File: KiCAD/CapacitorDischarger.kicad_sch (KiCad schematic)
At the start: 44 parts, among them J1 SLB4-G-21, J2 SLB4-G-22, J3 MKDS5/2-9.5, J4 MKDS5/2-9.5, J5 DVM_Connector, Q1 MPSA42, Q2 STP10NK80Z 800V 9A

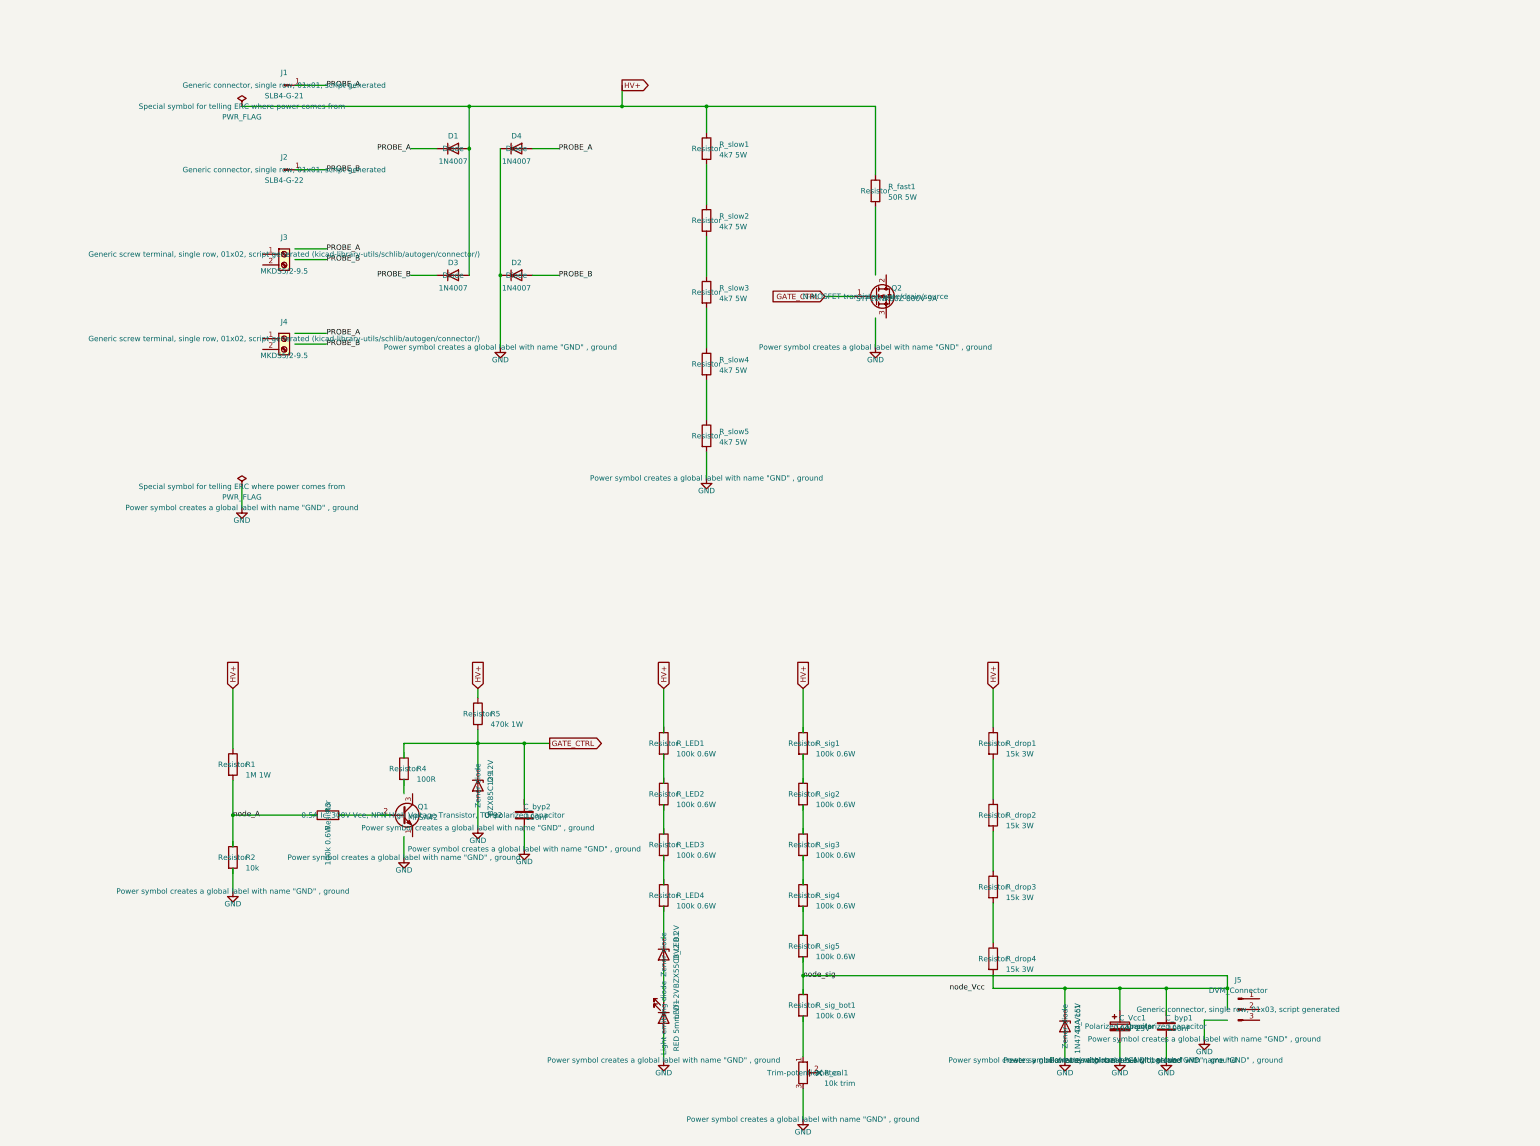
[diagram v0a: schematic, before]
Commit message: Design review fixes: fuse F1, battery-powered DVM, R3=10k, KiCad polarity fixes
Review of the full design (schematic, BOM, simulations) surfaced and fixed:

- Add F1 protection fuse (2A/600V KLKD002.T + Keystone 3517 clips) in
  series after the bridge — opens on single-fault Q2-stuck-on (~12A).
- Reduce R3 100k -> 10k: Q1 threshold now hFE-independent, 63V nominal /
  68V at the BF=40 corner (was 76V / 154V, peak I_fast ~3A over the 2A
  PCB limit).
- Replace the DVM Vcc parasitic dropper (4x15k + 1N4744A) with a 9V
  battery (BT1, holder w/ switch) via new polarized JST XH input J6:
  the sourced DVM module measures 12-15mA, beyond the dropper's 9.75mA.
- Fix gate-drive drawing in the generated schematic: D9 is a shunt clamp
  at GATE_CTRL, not in series (SVG previously showed a broken topology).
- KiCad root schematic: bridge D1-D4 and LED1 were mounted reversed —
  rotated 180 (netlist-verified); F1 and J6 added, dropper removed,
  VCC_DVM rail unshorted from node_sig, C_byp1 pins actually connected;
  value fields R3/R5/R_fast corrected; section drafts updated to match.
- Simulations: bridge D1-D4 now modeled (residual ~1V verified), MOSFET
  model renamed to STP10NK80Z, low-hFE threshold corner scenario G2
  added, Vcc branch removed with the dropper; suite passes 8/8.
- BOM/README: regenerate stale bom.md (Q1=MPSA42, 4x R_LED, 10k R_cal),
  correct stress-math notes, document residual voltage, threshold range,
  discharge time 45.5s @ 600V/1mF, and high-efficiency LED requirement.

Co-Authored-By: Claude Fable 5 <noreply@anthropic.com>
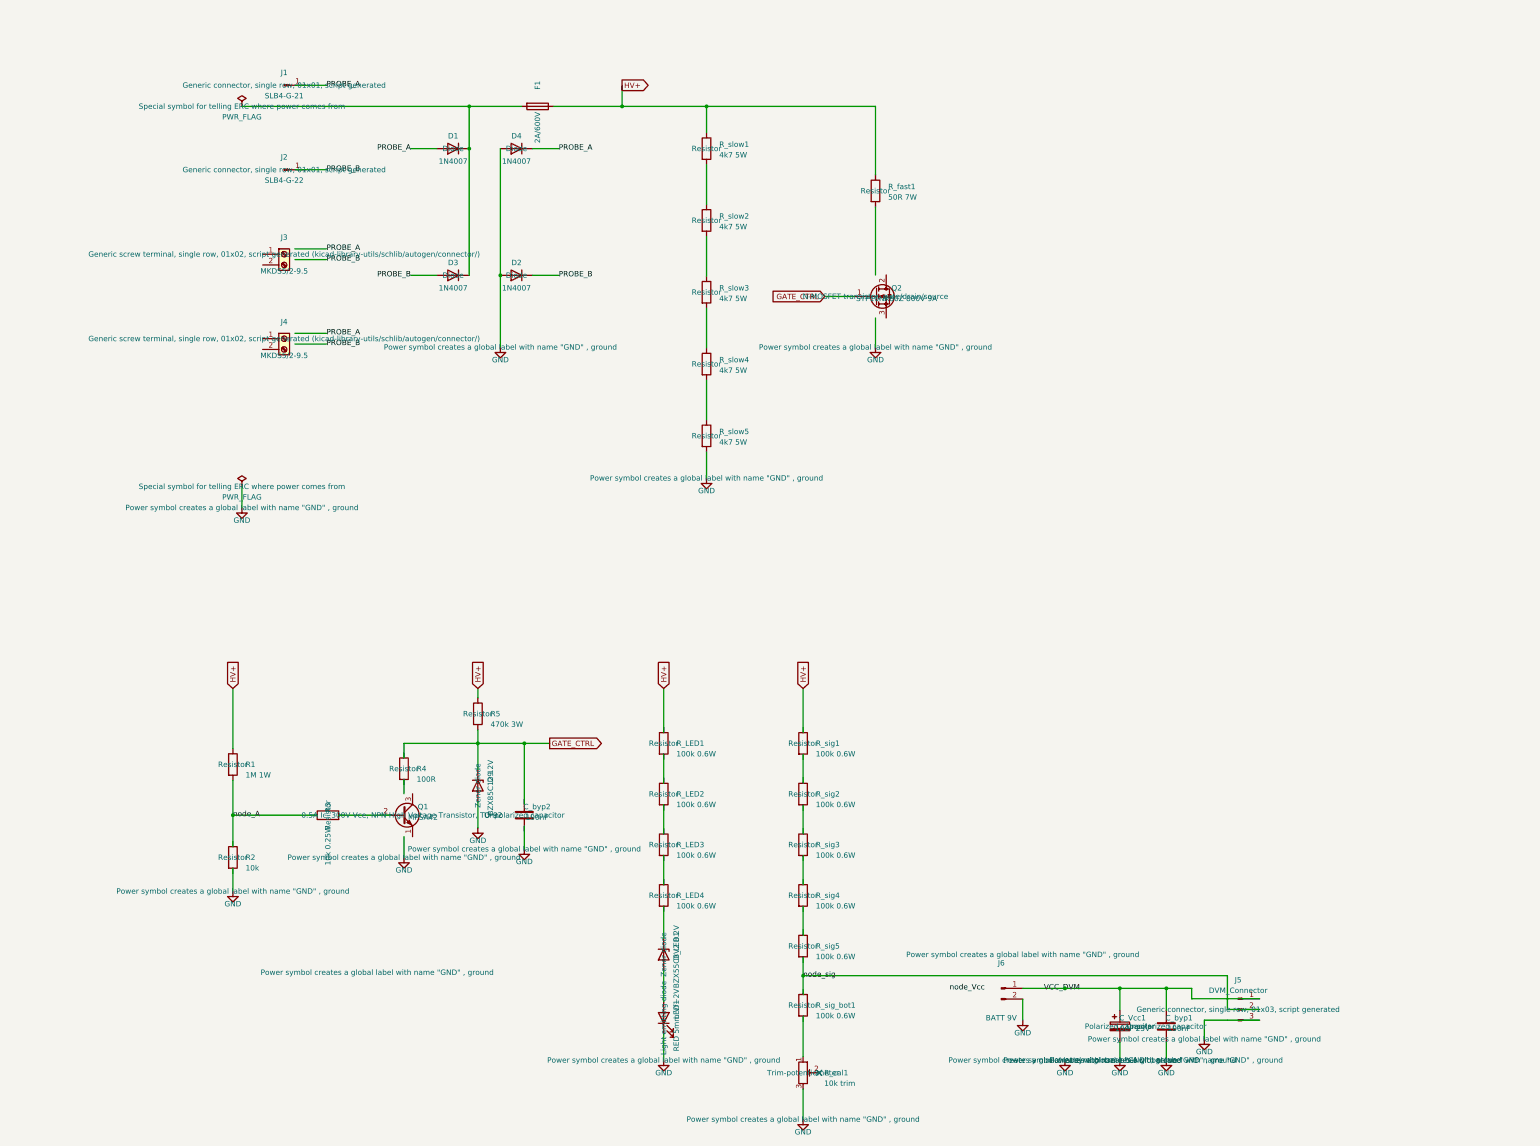
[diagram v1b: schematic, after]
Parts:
- removed D_Vcc1: 1N4744A 15V, Diode_THT:D_DO-41_SOD81_P10.16mm_Horizontal, symbol Device:D_Zener
- removed R_drop1, R_drop2, R_drop3, R_drop4: 15k 3W, Resistor_THT:R_Axial_DIN0516_L15.5mm_D5.0mm_P20.32mm_Horizontal, symbol Device:R
- added F1: 2A/600V, Fuse:Fuseholder_Clip-6.3x32mm_Littelfuse_102_Inline_P34.21x7.62mm_D2.54mm_Horizontal, symbol Device:Fuse
- added J6: BATT 9V, Connector_JST:JST_XH_B2B-XH-A_1x02_P2.50mm_Vertical, symbol Connector:Conn_01x02_Pin
- R3: value 100k 0.6W -> 10k 0.25W
- R5: value 470k 1W -> 470k 3W
- R_fast1: value 50R 5W -> 50R 7W
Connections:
- net GND: now also C_byp1.2, D2.2 (A), D4.2 (A), J5.3 (Pin_3), LED1.1 (K), J6.2 (Pin_2); no longer D2.1 (K), D4.1 (K), LED1.2 (A)
- net HV+: now also F1.2; no longer D1.2 (A), D3.2 (A)
- net PROBE_A: now also D1.2 (A), D4.1 (K); no longer D1.1 (K), D4.2 (A)
- net PROBE_B: now also D2.1 (K), D3.2 (A); no longer D2.2 (A), D3.1 (K)
- net node_sig: now also J5.2 (Pin_2); no longer C_Vcc1.1
- net at D_LED1.2 (A): now also LED1.2 (A); no longer LED1.1 (K)
- net VCC_DVM: now reaches C_byp1.1
- net VCC_DVM: now also C_Vcc1.1, J5.1 (Pin_1), J6.1 (Pin_1)
- new net: D1.1 (K), D3.1 (K), F1.1
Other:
- moved on the sheet: D1, D2, D3, D4, LED1

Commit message: Design review fixes, PM-128 voltmeter, TF1 cutoff, regenerated KiCad project
Circuit / simulation
- Add TF1 thermal cutoff (SEFUSE SF129R0, 133 °C) between R_fast and Q2;
  behavioural thermal model in the sim, live-supply scenario L
- Replace the 0-100 V DVM module with an Axiomet PM-128 (200 mV FS) on a
  10 000:1 divider (5 x 100k over 2 x 100R), D_clamp input protection,
  floating 9 V battery
- New scenarios: hFE/temperature corners (G3/G4), PM-128 divider (H),
  reverse polarity (I), hot-plug (J), 47 mF dump (K), live supply (L);
  run_sim fails on any ngspice error; 15/15 PASS

BOM
- F1 = ESKA 1038820 + Schurter CSO clips, R_sig_bot = 2 x 100R, HLMP-4700,
  HS-S01 heatsink, MST 220 insulator, wire, enclosure; TO_BUY_list.csv

KiCad (all generated by scripts in KiCAD/)
- gen_kicad_sch.py: flat schematic, netlist checked against the SPICE
  circuit by check_kicad.py (ERC clean)
- hv_rules.py: clearance = 1 mm per 100 V of worst-case voltage difference
  (6 mm HV to GND/LV)
- gen_pcb.py: 2-layer board 120 x 90 mm, Freerouting with per-net classes
- board_1s.py: single-sided 100 x 75 mm board for Bungard FEPCU-075,
  hand-routed, GND ring, no jumpers; fab_1s/ exposure PDF, drill, STEP
- gen_footprints.py / gen_3d.py: custom footprints and STEP bodies
- Remove the old hv_section / lv_section drafts

Co-Authored-By: Claude Opus 5.5 (1M context) <noreply@anthropic.com>
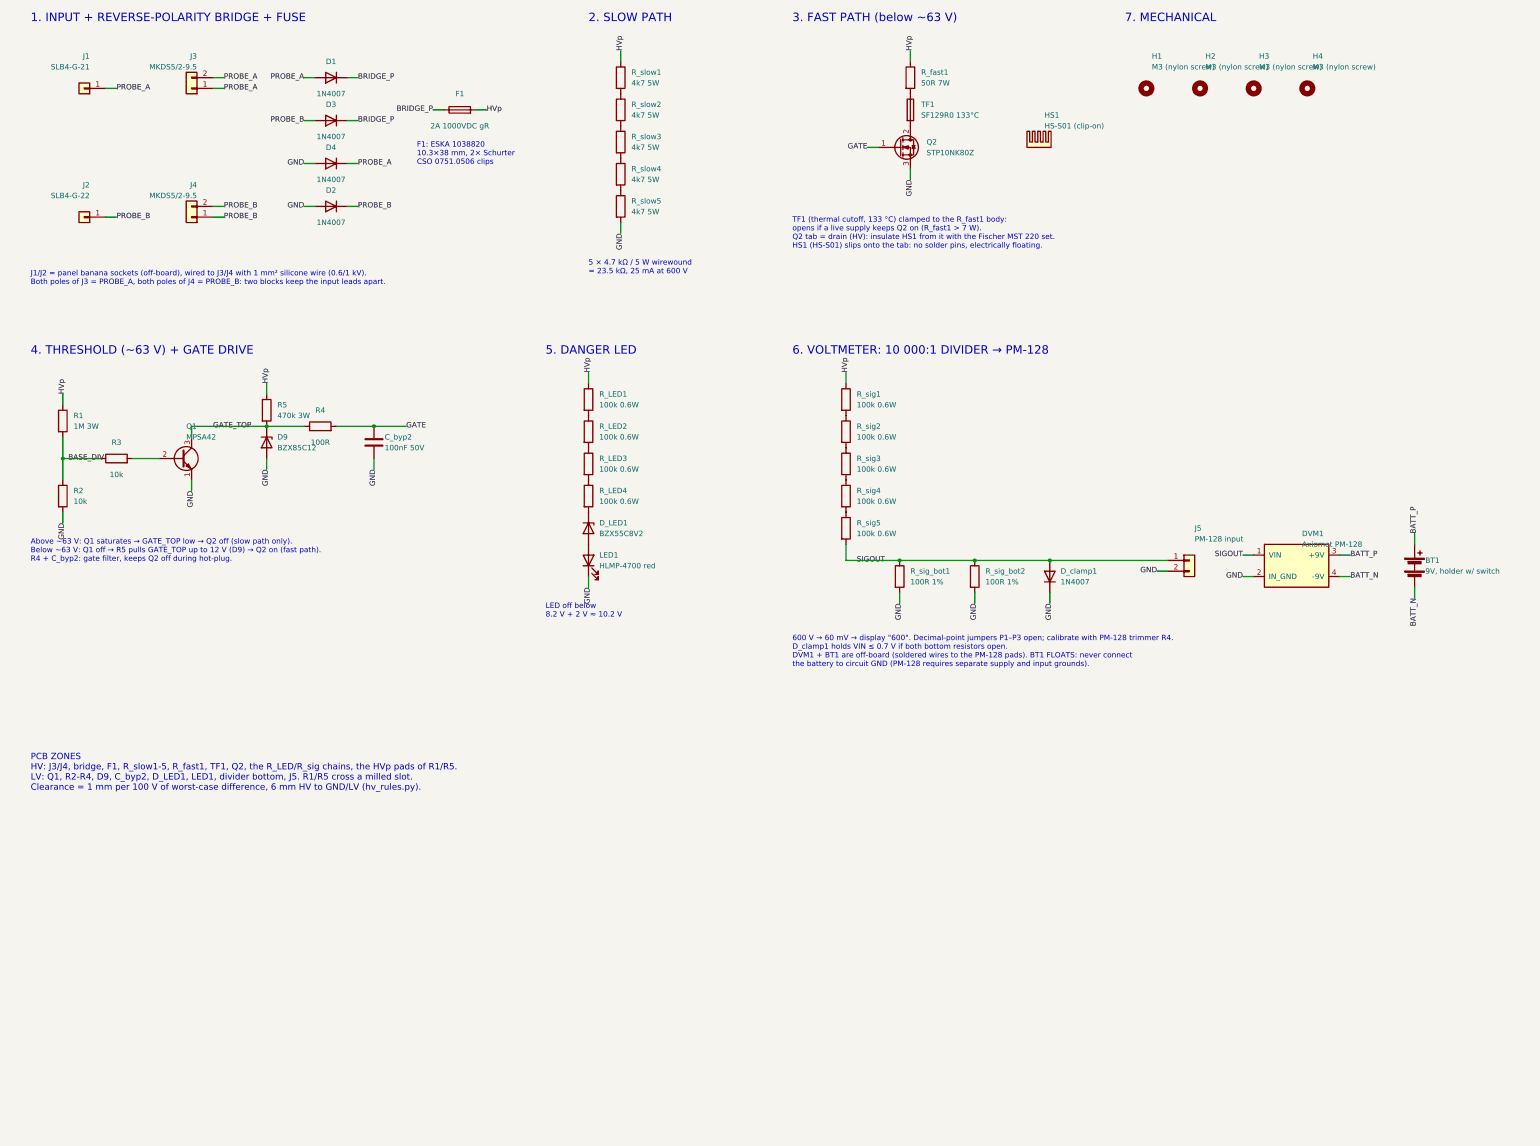
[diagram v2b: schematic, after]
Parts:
- removed C_Vcc1: 10uF 25V, Capacitor_THT:CP_Radial_D4.0mm_P2.00mm, symbol Device:C_Polarized
- removed C_byp1: 100nF, Capacitor_THT:C_Disc_D3.8mm_W2.6mm_P2.50mm, symbol Device:C
- removed J1: SLB4-G-21, Connector_PinHeader_2.54mm:PinHeader_1x01_P2.54mm_Vertical, symbol Connector:Conn_01x01_Pin
- removed J2: SLB4-G-22, Connector_PinHeader_2.54mm:PinHeader_1x01_P2.54mm_Vertical, symbol Connector:Conn_01x01_Pin
- removed J3, J4: MKDS5/2-9.5, TerminalBlock_Phoenix:TerminalBlock_Phoenix_MKDS-1,5-2_1x02_P5.00mm_Horizontal, symbol Connector:Screw_Terminal_01x02
- removed J5: DVM_Connector, Connector_PinHeader_2.54mm:PinHeader_1x03_P2.54mm_Vertical, symbol Connector:Conn_01x03_Pin
- removed J6: BATT 9V, Connector_JST:JST_XH_B2B-XH-A_1x02_P2.50mm_Vertical, symbol Connector:Conn_01x02_Pin
- removed Q1: MPSA42, Package_TO_SOT_THT:TO-92_Inline, symbol Transistor_BJT:MPSA42
- removed R_cal1: 10k trim, Potentiometer_THT:Potentiometer_Bourns_3296W_Vertical, symbol Device:R_Potentiometer_Trim
- added BT1: 9V, holder w/ switch, symbol Device:Battery
- added DVM1: Axiomet PM-128, symbol CapDis:PM-128
- added D_clamp1: 1N4007, Diode_THT:D_DO-41_SOD81_P5.08mm_Vertical_AnodeUp, symbol Device:D
- added H1, H2, H3, H4: M3 (nylon screw), MountingHole:MountingHole_3.2mm_M3, symbol Mechanical:MountingHole
- added HS1: HS-S01 (clip-on), symbol Mechanical:Heatsink
- added J1: SLB4-G-21, symbol Connector_Generic:Conn_01x01
- added J2: SLB4-G-22, symbol Connector_Generic:Conn_01x01
- added J3, J4: MKDS5/2-9.5, CapDis:TerminalBlock_Phoenix_MKDS-5-2-9.5_1x02_P9.52mm, symbol Connector_Generic:Conn_01x02
- added J5: PM-128 input, Connector_PinHeader_2.54mm:PinHeader_1x02_P2.54mm_Vertical, symbol Connector_Generic:Conn_01x02
- added Q1: MPSA42, Package_TO_SOT_THT:TO-92_Inline_Wide, symbol Transistor_BJT:Q_NPN_EBC
- added R_sig_bot2: 100R 1%, Resistor_THT:R_Axial_DIN0207_L6.3mm_D2.5mm_P2.54mm_Vertical, symbol Device:R
- added TF1: SF129R0 133°C, CapDis:ThermalCutoff_SEFUSE_SF_Axial, symbol Device:Fuse
- C_byp2: value 100nF -> 100nF 50V; footprint Capacitor_THT:C_Disc_D3.8mm_W2.6mm_P2.50mm -> Capacitor_THT:C_Disc_D5.0mm_W2.5mm_P5.00mm; MPN (none) -> K104K10X7RF5UH5
- D1, D2, D3, D4: MPN (none) -> 1N4007 (Diotec, Mouser 637-1N4007)
- D9: value BZX85C12 12V -> BZX85C12; footprint Diode_THT:D_DO-41_SOD81_P10.16mm_Horizontal -> Diode_THT:D_DO-41_SOD81_P5.08mm_Vertical_AnodeUp; MPN (none) -> BZX85C12 (onsemi, Mouser 512-BZX85C12)
- D_LED1: value BZX55C8V2 8.2V -> BZX55C8V2; footprint Diode_THT:D_DO-35_SOD27_P7.62mm_Horizontal -> Diode_THT:D_DO-35_SOD27_P5.08mm_Vertical_AnodeUp; MPN (none) -> BZX55C8V2-TAP (Vishay, Mouser 78-BZX55C8V2-TAP)
- F1: value 2A/600V -> 2A 1000VDC gR; footprint Fuse:Fuseholder_Clip-6.3x32mm_Littelfuse_102_Inline_P34.21x7.62mm_D2.54mm_Horizontal -> CapDis:Fuseholder_Clip-10.3x38mm_Schurter_CSO_0751.0506; MPN (none) -> ESKA 1038820 (TME 1038820, in stock 2026-10-01; alt DF ELEC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
- LED1: value RED 5mm Vf~2V -> HLMP-4700 red; MPN (none) -> HLMP-4700 (Broadcom, low-current red, TME HLMP-4700) — fall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
- Q2: value STP10NK80Z 800V 9A -> STP10NK80Z; footprint Package_TO_SOT_THT:TO-220-3_Vertical -> CapDis:TO-220-3_Vertical_LegsSpread_P5.08mm; MPN (none) -> STP10NK80Z (alt: STF7NM80, IXTP2N80)
- R1: value 1M 1W -> 1M 3W; footprint Resistor_THT:R_Axial_DIN0516_L15.5mm_D5.0mm_P20.32mm_Horizontal -> CapDis:R_Axial_DIN0516_L15.5mm_D5.0mm_P10.16mm_Vertical_BodyOnPad2; MPN (none) -> FMP300FRF73-1M (YAGEO, Mouser 603-FMP300FRF73-1M)
- R2: footprint Resistor_THT:R_Axial_DIN0207_L6.3mm_D2.5mm_P10.16mm_Horizontal -> Resistor_THT:R_Axial_DIN0207_L6.3mm_D2.5mm_P2.54mm_Vertical; MPN (none) -> MFR-25FTE52-10K (YAGEO, Mouser 603-MFR-25FTE52-10K)
- R3: value 10k 0.25W -> 10k; footprint Resistor_THT:R_Axial_DIN0207_L6.3mm_D2.5mm_P10.16mm_Horizontal -> Resistor_THT:R_Axial_DIN0207_L6.3mm_D2.5mm_P2.54mm_Vertical; MPN (none) -> MFR-25FTE52-10K (YAGEO, Mouser 603-MFR-25FTE52-10K)
- R4: footprint Resistor_THT:R_Axial_DIN0207_L6.3mm_D2.5mm_P10.16mm_Horizontal -> Resistor_THT:R_Axial_DIN0207_L6.3mm_D2.5mm_P2.54mm_Vertical; MPN (none) -> RN60D1000FB14 (Vishay, Mouser 71-RN60D-F-100)
- R5: footprint Resistor_THT:R_Axial_DIN0516_L15.5mm_D5.0mm_P20.32mm_Horizontal -> CapDis:R_Axial_DIN0516_L15.5mm_D5.0mm_P10.16mm_Vertical_BodyOnPad2; MPN (none) -> FMP300FRF73-470K (YAGEO, Mouser 603-FMP300FRF73-470K)
- R_LED1, R_LED2, R_LED3, R_LED4, R_sig1, R_sig2, R_sig3, R_sig4, R_sig5: footprint Resistor_THT:R_Axial_DIN0207_L6.3mm_D2.5mm_P10.16mm_Horizontal -> Resistor_THT:R_Axial_DIN0207_L6.3mm_D2.5mm_P5.08mm_Vertical; MPN (none) -> MF006FF1003A50
- R_fast1: footprint Resistor_THT:R_Axial_Power_L38.0mm_W9.0mm_P40.64mm -> CapDis:R_Axial_Ohmite_27J_7W; MPN (none) -> 27J50RE (Ohmite, Mouser 588-27J50RE)
- R_sig_bot1: value 100k 0.6W -> 100R 1%; footprint Resistor_THT:R_Axial_DIN0207_L6.3mm_D2.5mm_P10.16mm_Horizontal -> Resistor_THT:R_Axial_DIN0207_L6.3mm_D2.5mm_P2.54mm_Vertical; MPN (none) -> YAGEO MF0207FTE52-100R (TME MF0207FTE-100R; any 100 Ω 1% me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
- R_slow1, R_slow2, R_slow3, R_slow4, R_slow5: footprint Resistor_THT:R_Axial_Power_L25.0mm_W9.0mm_P30.48mm -> CapDis:R_Axial_Ohmite_45F_5W; MPN (none) -> 45F4K7E (Ohmite, Mouser 588-45F4K7E)
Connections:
- net HV+ is gone; now on net HVp: F1.2, R1.1, R5.1, R_fast1.1, R_slow1.1
- net node_A is gone; now on net BASE_DIV: R1.2
- net GND: now also C_byp2.2, Q2.3 (S), R2.2, R_sig_bot1.2, DVM1.2 (IN_GND), D_clamp1.1 (K), J5.2 (Pin_2), Q1.1 (E), R_sig_bot2.2
- net PROBE_A: now also J1.1 (Pin_1), J3.1 (Pin_1), J3.2 (Pin_2)
- net PROBE_B: now also J2.1 (Pin_1), J4.1 (Pin_1), J4.2 (Pin_2)
- net BRIDGE_P: now reaches D1.1 (K), D3.1 (K), F1.1
- net at R_fast1.2: now also TF1.1
- net at Q2.2 (D): now also TF1.2
- net BASE_DIV: now reaches R2.1
- net BASE_DIV: now also R3.1
- net at R3.2: now also Q1.2 (B)
- net GATE_TOP: now reaches R4.1
- net GATE_TOP: now also D9.1 (K), R5.2, Q1.3 (C)
- net GATE: now reaches R4.2
- net GATE: now also C_byp2.1, Q2.1 (G)
- net HVp: now reaches R_LED1.1
- net HVp: now also R_sig1.1
- net at R_LED1.2: now also R_LED2.1
- net at R_LED2.2: now also R_LED3.1
- net at R_LED3.2: now also R_LED4.1
- net at R_LED4.2: now also D_LED1.1 (K)
- net at R_sig1.2: now also R_sig2.1
- net at R_sig2.2: now also R_sig3.1
- net at R_sig3.2: now also R_sig4.1
- net at R_sig4.2: now also R_sig5.1
- net SIGOUT: now reaches R_sig5.2
- net SIGOUT: now also R_sig_bot1.1, DVM1.1 (VIN), D_clamp1.2 (A), J5.1 (Pin_1), R_sig_bot2.1
- removed net GATE_CTRL: D9.1 (K), Q2.1 (G), R5.2
- new net BATT_N: BT1.2 (-), DVM1.4 (-9V)
- new net BATT_P: BT1.1 (+), DVM1.3 (+9V)
- no-connect marks 1 -> 0
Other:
- note added: "1. INPUT + REVERSE-POLARITY BRIDGE + FUSE"
- note added: "2. SLOW PATH"
- note added: "3. FAST PATH (below ~63 V)"
- note added: "4. THRESHOLD (~63 V) + GATE DRIVE"
- note added: "5 × 4.7 kΩ / 5 W wirewound = 23.5 kΩ, 25 mA at 600 V"
- note added: "5. DANGER LED"
- note added: "6. VOLTMETER: 10 000:1 DIVIDER → PM-128"
- note added: "600 V → 60 mV → display "600". Decimal-point jumpers P1–P3 open; calibrate with PM-128 trimmer R4. D_clamp1 holds VIN ≤ 0.7 V if both bottom resistors open. DVM1 + BT1 are off-board (soldered wires to the PM-128 pads). BT1 FLOATS: never connect the battery to circuit GND (PM-128 requires separate supply and input grounds)."
- note added: "7. MECHANICAL"
- note added: "Above ~63 V: Q1 saturates → GATE_TOP low → Q2 off (slow path only). Below ~63 V: Q1 off → R5 pulls GATE_TOP up to 12 V (D9) → Q2 on (fast path). R4 + C_byp2: gate filter, keeps Q2 off during hot-plug."
- note added: "F1: ESKA 1038820 10.3×38 mm, 2× Schurter CSO 0751.0506 clips"
- note added: "J1/J2 = panel banana sockets (off-board), wired to J3/J4 with 1 mm² silicone wire (0.6/1 kV). Both poles of J3 = PROBE_A, both poles of J4 = PROBE_B: two blocks keep the input leads apart."
- note added: "LED off below 8.2 V + 2 V ≈ 10.2 V"
- note added: "PCB ZONES HV: J3/J4, bridge, F1, R_slow1-5, R_fast1, TF1, Q2, the R_LED/R_sig chains, the HVp pads of R1/R5. LV: Q1, R2-R4, D9, C_byp2, D_LED1, LED1, divider bottom, J5. R1/R5 cross a milled slot. Clearance = 1 mm per 100 V of worst-case difference, 6 mm HV to GND/LV (hv_rules.py)."
- note added: "TF1 (thermal cutoff, 133 °C) clamped to the R_fast1 body: opens if a live supply keeps Q2 on (R_fast1 > 7 W). Q2 tab = drain (HV): insulate HS1 from it with the Fischer MST 220 set. HS1 (HS-S01) slips onto the tab: no solder pins, electrically floating."
